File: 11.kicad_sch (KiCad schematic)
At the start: 3 parts, among them U23 AM6442BSFGHAALV

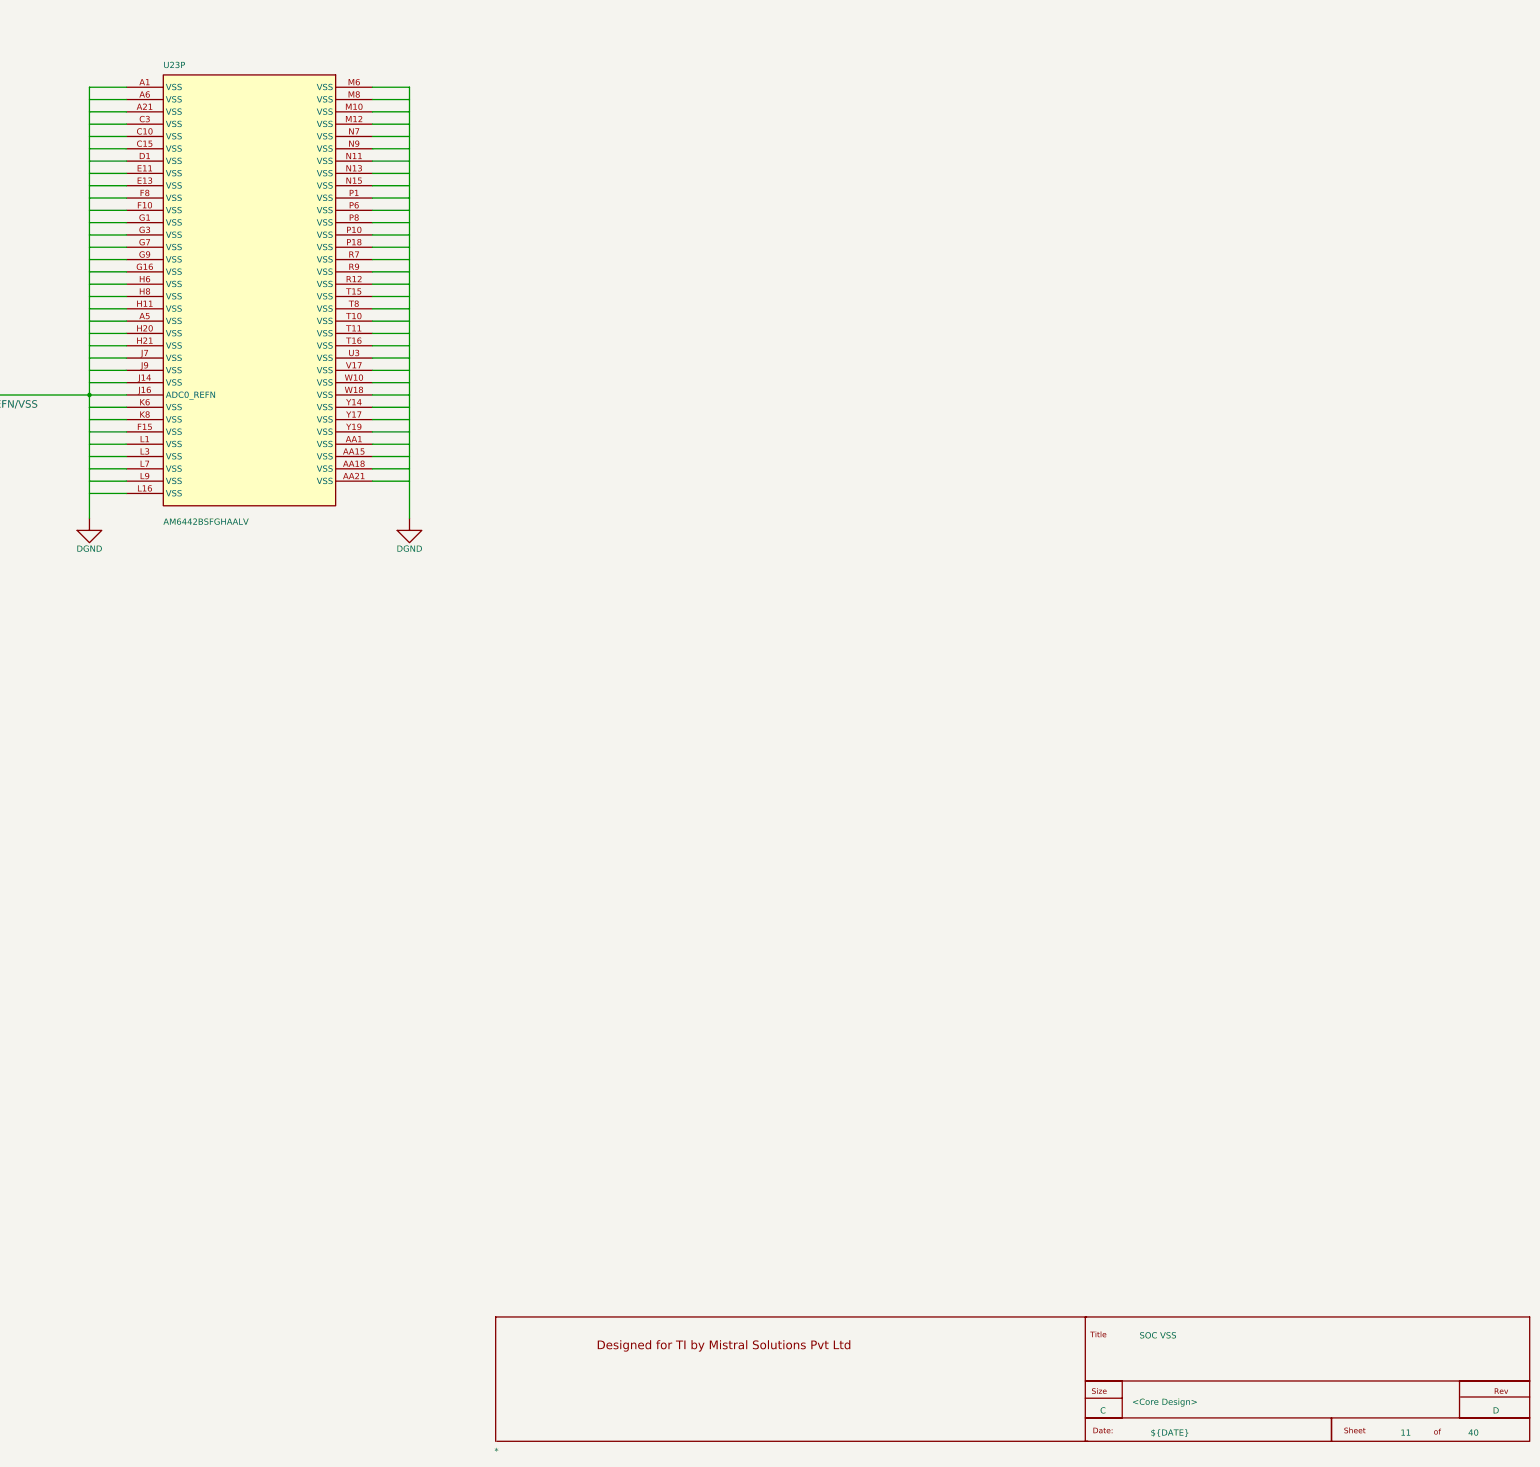
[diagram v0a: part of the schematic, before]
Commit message: fix joint, offpage, and typo
DRC errors are cleared, some warnings remain.
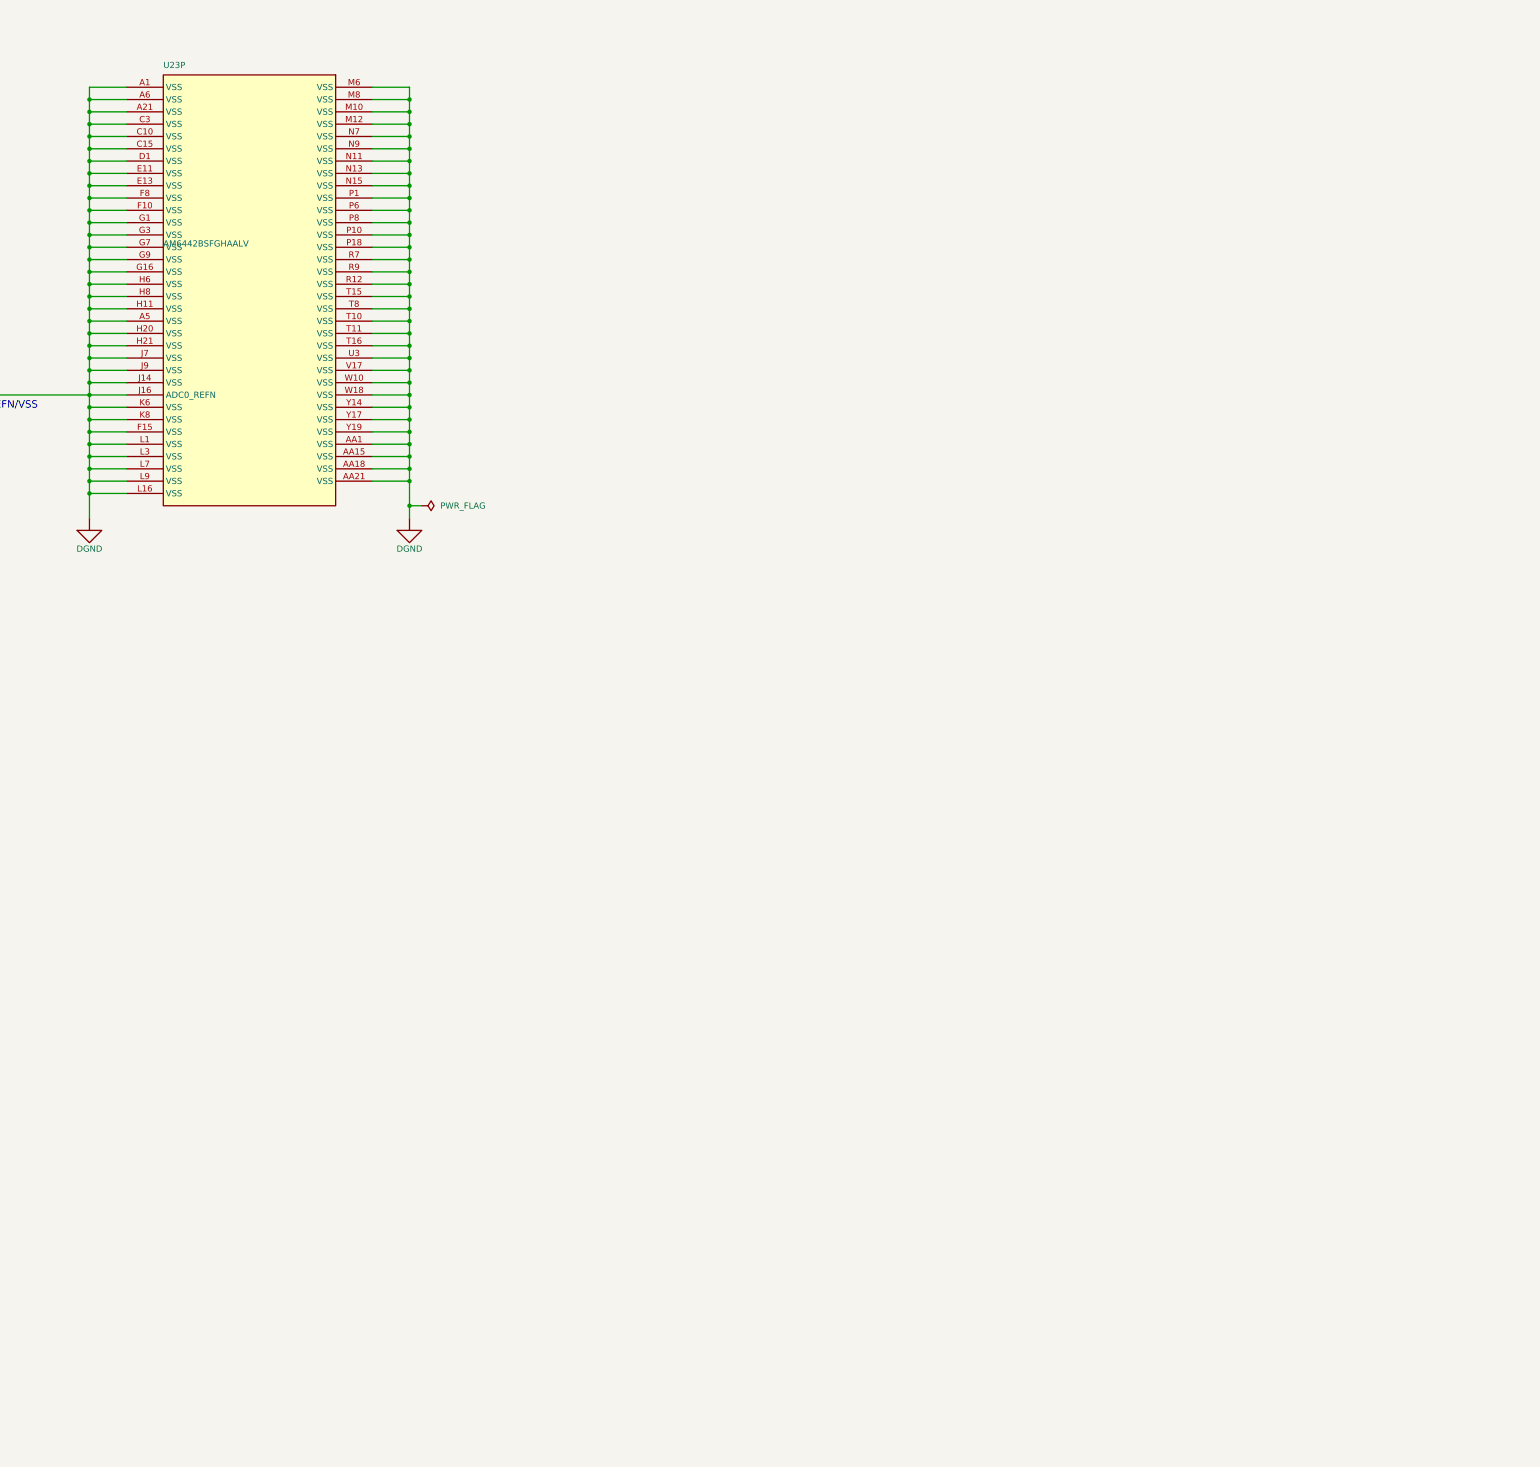
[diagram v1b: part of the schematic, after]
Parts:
- removed *: MISTRAL_TITLEBLK_CSIZE, symbol 11-altium-import:root_0_MISTRAL_TITLEBLK_CSIZE
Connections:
- net DGND: now also U23.A21 (VSS), U23.A5 (VSS), U23.A6 (VSS), U23.AA1 (VSS), U23.AA15 (VSS), U23.AA18 (VSS), U23.AA21 (VSS), U23.C10 (VSS), U23.C15 (VSS), U23.C3 (VSS), U23.D1 (VSS), U23.E11 (VSS), U23.E13 (VSS), U23.F10 (VSS), U23.F15 (VSS), U23.F8 (VSS), U23.G1 (VSS), U23.G16 (VSS), U23.G3 (VSS), U23.G7 (VSS), U23.G9 (VSS), U23.H11 (VSS), U23.H20 (VSS), U23.H21 (VSS), U23.H6 (VSS), U23.H8 (VSS), U23.J14 (VSS), U23.J7 (VSS), U23.J9 (VSS), U23.K8 (VSS), U23.L1 (VSS), U23.L16 (VSS), U23.L3 (VSS), U23.L7 (VSS), U23.L9 (VSS), U23.M10 (VSS), U23.M12 (VSS), U23.M8 (VSS), U23.N11 (VSS), U23.N13 (VSS), U23.N15 (VSS), U23.N7 (VSS), U23.N9 (VSS), U23.P1 (VSS), U23.P10 (VSS), U23.P18 (VSS), U23.P6 (VSS), U23.P8 (VSS), U23.R12 (VSS), U23.R7 (VSS), U23.R9 (VSS), U23.T10 (VSS), U23.T11 (VSS), U23.T15 (VSS), U23.T16 (VSS), U23.T8 (VSS), U23.U3 (VSS), U23.V17 (VSS), U23.W10 (VSS), U23.W18 (VSS), U23.Y14 (VSS), U23.Y17 (VSS), U23.Y19 (VSS)

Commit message: a lot, mpu power almost ready.
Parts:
- removed C541: 0.1uF, CAP0201_0-5, symbol 11-altium-import:root_0_CAP_Dup3
- added C541: 100n,10%,10V, Abacus:C_0201_0603Metric_0.64x0.32mm_Courtyard, symbol JLCE_C0201:100n,10%,10V
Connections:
- net DGND: now also C541.2
- new net VDDA_ADC: C541.1
